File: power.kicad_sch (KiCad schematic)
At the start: 53 parts, among them J2 USB3_B, U4 TPS563201DDCR, U5 TPS563201DDCR, U6 TPS563201DDCR, U7 TLV75519PDBVR, U8 TLV75519PDBVR, U9 TLV75733PDBVR

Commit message: Footprints: TVP7002 pad and vias per the OSSC, FX3 pads per AN70707; spare boot EEPROM
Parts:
- removed U4: TPS563201DDCR, ps1-av-capture:SOT-23-6_L2.9-W1.6-P0.95-LS2.8-BR, symbol Regulator_Switching:TPS563201
- removed U7: TLV75519PDBVR, Package_TO_SOT_SMD:SOT-23-5, symbol Regulator_Linear:TLV75519PDBV
- removed U9: TLV75733PDBVR, Package_TO_SOT_SMD:SOT-23-5, symbol Regulator_Linear:TLV75733PDBV
- added U10: TLV75733PDBVR, Package_TO_SOT_SMD:SOT-23-5, symbol Regulator_Linear:TLV75733PDBV
- added U7: TPS563201DDCR, ps1-av-capture:SOT-23-6_L2.9-W1.6-P0.95-LS2.8-BR, symbol Regulator_Switching:TPS563201
- added U9: TLV75519PDBVR, Package_TO_SOT_SMD:SOT-23-5, symbol Regulator_Linear:TLV75519PDBV
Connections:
- net +1V9A: now also U8.5 (OUT)
- net +1V9D: now also U9.5 (OUT); no longer U8.5 (OUT)
- net +2V5: now also U9.1 (IN), U9.3 (EN)
- net +3V3A: now also U10.5 (OUT)
- net BST_1V2: now also U7.6 (VBST); no longer U6.6 (VBST)
- net BST_2V5: now also U6.6 (VBST); no longer U5.6 (VBST)
- net BST_3V3: now also U5.6 (VBST)
- net EN_1V2: now also U7.5 (EN); no longer U6.5 (EN)
- net EN_2V5: now also U6.5 (EN); no longer U5.5 (EN)
- net EN_3V3: now also U5.5 (EN)
- net FB_1V2: now also U7.4 (VFB); no longer U6.4 (VFB)
- net FB_2V5: now also U6.4 (VFB); no longer U5.4 (VFB)
- net FB_3V3: now also U5.4 (VFB)
- net GND: now also U10.2 (GND), U7.1 (GND), U9.2 (GND)
- net SW_1V2: now also U7.2 (SW); no longer U6.2 (SW)
- net SW_2V5: now also U6.2 (SW); no longer U5.2 (SW)
- net SW_3V3: now also U5.2 (SW)
- net VBUS: now also U10.1 (IN), U10.3 (EN), U7.3 (VIN)

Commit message: Status LED: common-anode RGB on FX3 GPIO50-52, firmware state map
XL-1615RGBC-RF (C965840) replaces the GPIO57 debug LED. Its LCSC pattern
numbers G and B the other way from the datasheet; fix_footprints.py renumbers
them and applies the datasheet's land pattern. GPIO budget in docs/design.md.
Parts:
- removed R52, R53: 100k, Resistor_SMD:R_0402_1005Metric, symbol Device:R
- added R63: 10k, Resistor_SMD:R_0402_1005Metric, symbol Device:R
- added R64: 1k, Resistor_SMD:R_0402_1005Metric, symbol Device:R
- R54: value 33.2k 1% -> 100k; LCSC C122548 -> C25741
- R55, R58, R61: value 10k -> 100k; LCSC C25744 -> C25741
- R56: value 100k -> 33.2k 1%; LCSC C25741 -> C122548
- R57: value 22.6k 1% -> 10k; LCSC C26960 -> C25744
- R59: value 100k -> 22.6k 1%; LCSC C25741 -> C26960
- R60: value 5.76k 1% -> 10k; LCSC C5153969 -> C25744
- R62: value 1k -> 5.76k 1%; LCSC C11702 -> C5153969
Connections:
- net +1V2: now also R62.1; no longer R60.1
- net +2V5: now also R59.1; no longer R57.1
- net +3V3: now also R56.1; no longer R54.1
- net EN_1V2: now also R61.2; no longer R59.2
- net EN_2V5: now also R58.2; no longer R56.2
- net EN_3V3: now also R55.2
- net FB_1V2: now also R62.2, R63.1; no longer R60.2, R61.1
- net FB_2V5: now also R59.2, R60.1; no longer R57.2, R58.1
- net FB_3V3: now also R56.2, R57.1; no longer R54.2, R55.1
- net GND: now also R54.2, R57.2, R60.2, R63.2, R64.2; no longer R55.2, R58.2, R61.2, R62.2
- net PWR_LED_K: now also R64.1; no longer R62.1
- net USB3_SHIELD: now also R54.1
- net VBUS: now also R55.1, R58.1, R61.1; no longer R56.1, R59.1

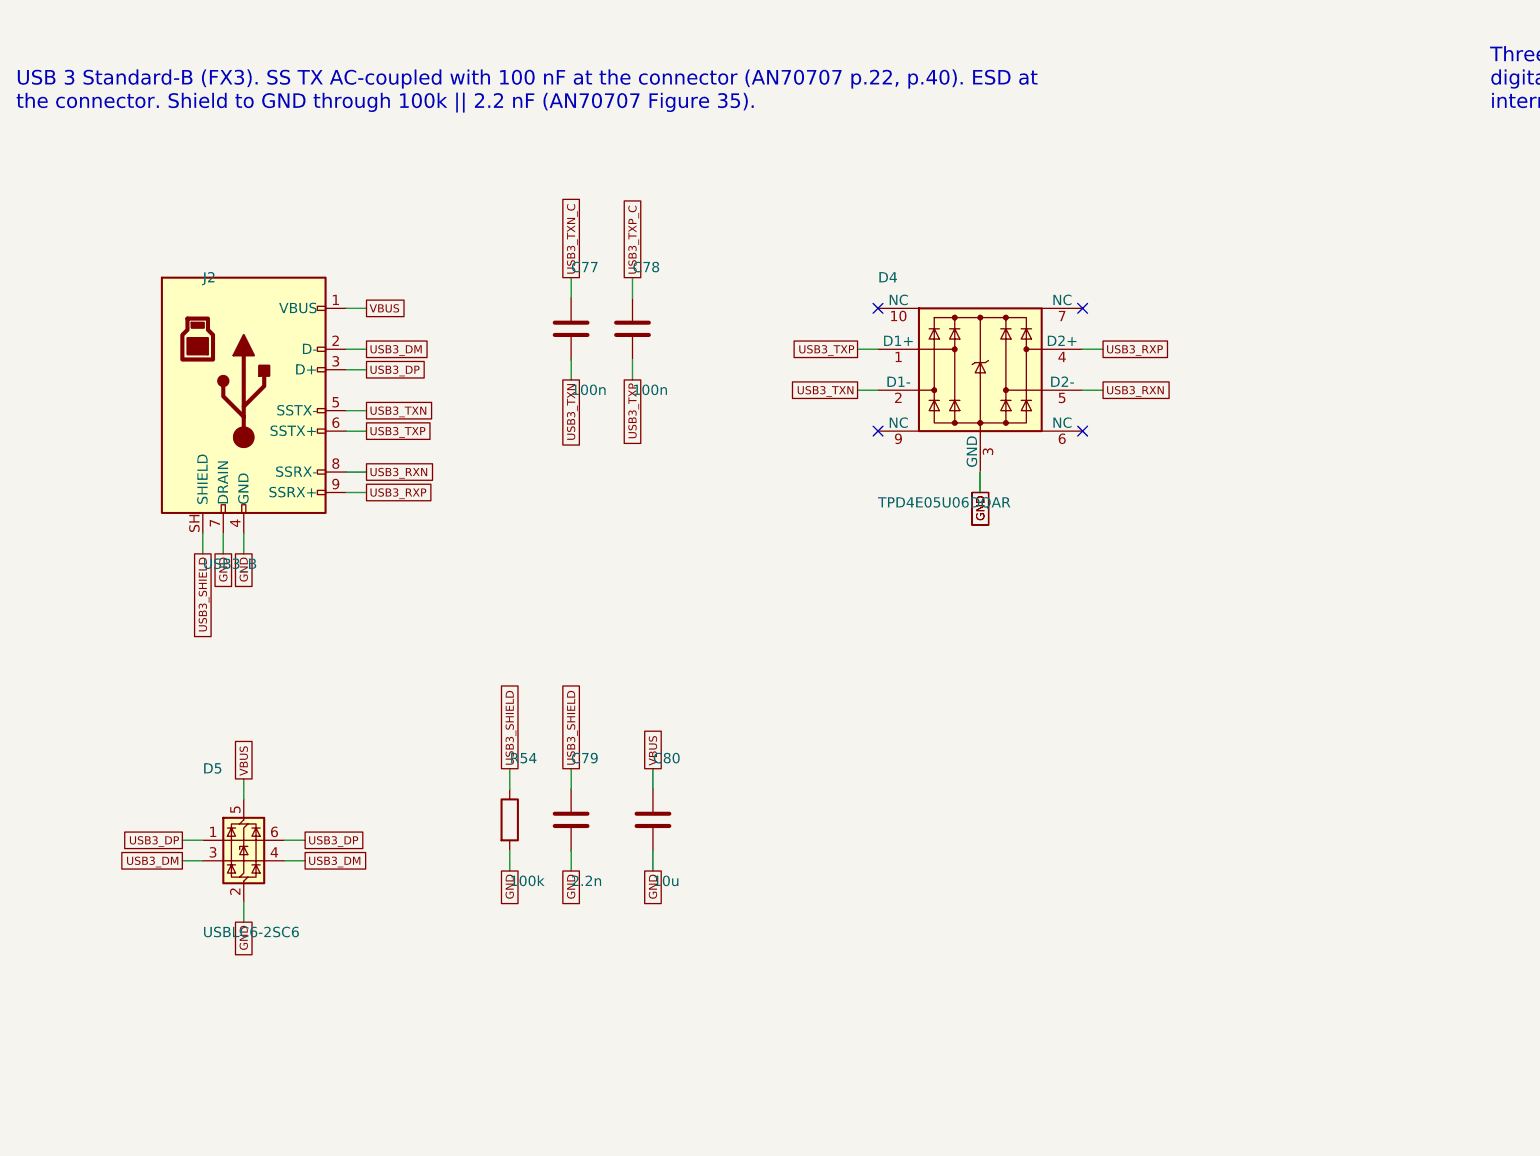
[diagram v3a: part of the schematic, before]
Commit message: Layout: USB 3 corridor placed and routed, pairs length-matched
SS TX/RX on L1 from the FX3's row A through one flow-through TPD4E05U06 to
the receptacle; RX wired P-to-N as AN70707 p.22 allows. D+/D- through the
USBLC6, then L4. route_usb.py matches each pair by 45-degree bumps and prints
the lengths; L2 GND plane added.
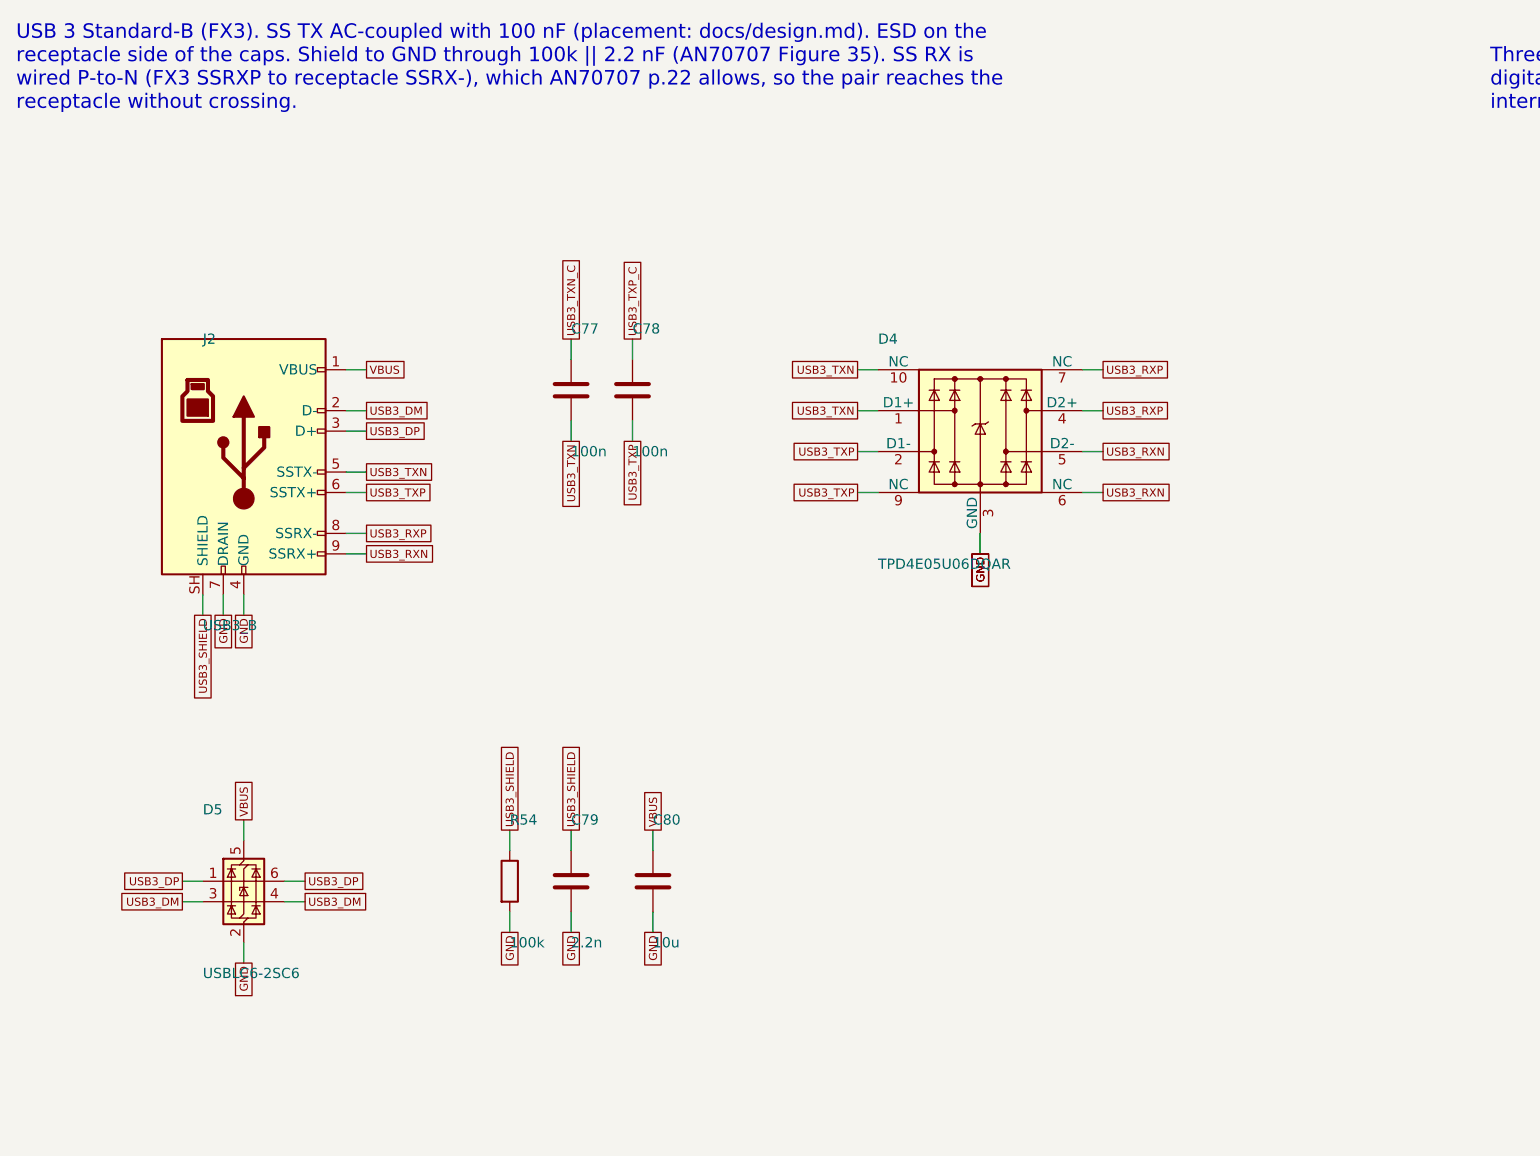
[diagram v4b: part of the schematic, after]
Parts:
- D4: Note (none) -> Flow-through: each channel's NC pad opposite (10/9/7/6) car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
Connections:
- net USB3_RXN: now also D4.6 (NC), J2.9 (SSRX+); no longer J2.8 (SSRX-)
- net USB3_RXP: now also D4.7 (NC), J2.8 (SSRX-); no longer J2.9 (SSRX+)
- net USB3_TXN: now also D4.1 (D1+), D4.10 (NC); no longer D4.2 (D1-)
- net USB3_TXP: now also D4.2 (D1-), D4.9 (NC); no longer D4.1 (D1+)
- no-connect marks 7 -> 3
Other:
- note added: "USB 3 Standard-B (FX3). SS TX AC-coupled with 100 nF (placement: docs/design.md). ESD on the receptacle side of the caps. Shield to GND through 100k || 2.2 nF (AN70707 Figure 35). SS RX is wired P-to-N (FX3 SSRXP to receptacle SSRX-), which AN70707 p.22 allows, so the pair reaches the receptacle without crossing."
- note removed: "USB 3 Standard-B (FX3). SS TX AC-coupled with 100 nF at the connector (AN70707 p.22, p.40). ESD at the connector. Shield to GND through 100k || 2.2 nF (AN70707 Figure 35)."
